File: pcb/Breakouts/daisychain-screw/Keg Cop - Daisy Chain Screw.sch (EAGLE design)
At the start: 4 parts

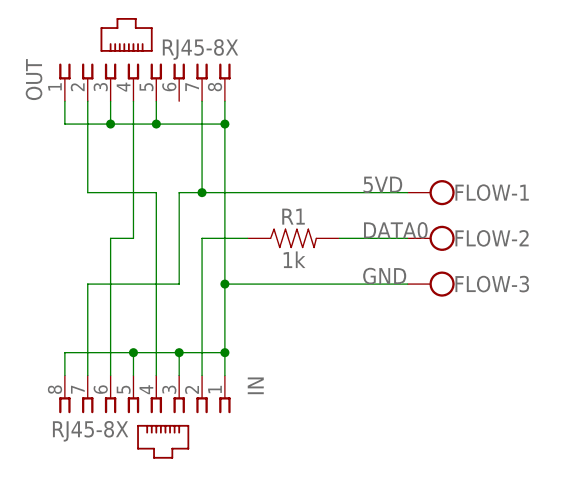
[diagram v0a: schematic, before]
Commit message: Reorganize daisy chain boards
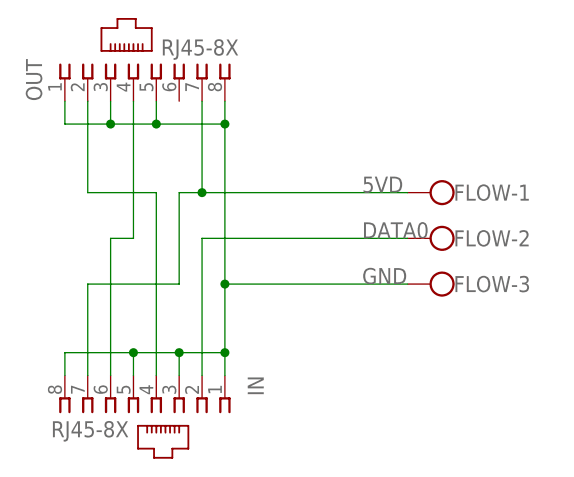
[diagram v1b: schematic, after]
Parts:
- removed R1: 1k, SparkFun-Resistors:1KOHM-HORIZ-1/4W-5%
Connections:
- removed net N$1: FLOW-2.KL, R1.2
- net DATA0: now also FLOW-2.KL; no longer R1.1
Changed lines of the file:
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@@
 <drawing>
 <settings>
-<setting alwaysvectorfont="yes"/>
+<setting alwaysvectorfont="no"/>
 <setting verticaltext="up"/>
 </settings>
@@
 <part name="OUT" library="con-tycoelectronics" library_urn="urn:adsk.eagle:library:193" deviceset="RJ45" device="" package3d_urn="urn:adsk.eagle:package:10660/1" technology="-8X"/>
 <part name="FLOW" library="con-wago-500" library_urn="urn:adsk.eagle:library:195" deviceset="W237-103" device="" package3d_urn="urn:adsk.eagle:package:10691/1"/>
-<part name="R1" library="SparkFun-Resistors" library_urn="urn:adsk.eagle:library:532" deviceset="1KOHM" device="-HORIZ-1/4W-5%" package3d_urn="urn:adsk.eagle:package:39658/1" value="1k"/>
 </parts>
 <sheets>
@@
 <attribute name="VALUE" x="99.06" y="49.403" size="1.778" layer="96" rot="R180"/>
 <attribute name="NAME" x="96.52" y="44.831" size="1.778" layer="95"/>
-</instance>
-<instance part="R1" gate="G$1" x="78.74" y="50.8" smashed="yes">
-<attribute name="NAME" x="78.74" y="52.324" size="1.778" layer="95" font="vector" align="bottom-center"/>
-<attribute name="VALUE" x="78.74" y="49.276" size="1.778" layer="96" font="vector" align="top-center"/>
 </instance>
 </instances>
@@
 <wire x1="68.58" y1="35.56" x2="68.58" y2="50.8" width="0.1524" layer="91"/>
 <label x="86.36" y="50.8" size="1.778" layer="95"/>
-<pinref part="R1" gate="G$1" pin="1"/>
-<wire x1="68.58" y1="50.8" x2="73.66" y2="50.8" width="0.1524" layer="91"/>
+<pinref part="FLOW" gate="-2" pin="KL"/>
+<wire x1="68.58" y1="50.8" x2="91.44" y2="50.8" width="0.1524" layer="91"/>
 </segment>
 </net>
@@
 </segment>
 </net>
-<net name="N$1" class="0">
-<segment>
-<pinref part="FLOW" gate="-2" pin="KL"/>
-<wire x1="91.44" y1="50.8" x2="83.82" y2="50.8" width="0.1524" layer="91"/>
-<pinref part="R1" gate="G$1" pin="2"/>
-</segment>
-</net>
